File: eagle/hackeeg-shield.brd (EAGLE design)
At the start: 101.6 x 53.3 mm, 144 parts, among them IC1 ADS1299IPAG, IC10 TXB0108PWR, IC11 TXB0108PWR, IC2 TPS72325DBVT, IC3 TPS73225DBVT, IC5 24AA256UID, IC6 TPS60403DBVT, IC7 OPA376DBV, IC8 OPA376DBV, IC9 TXS0102DCUR

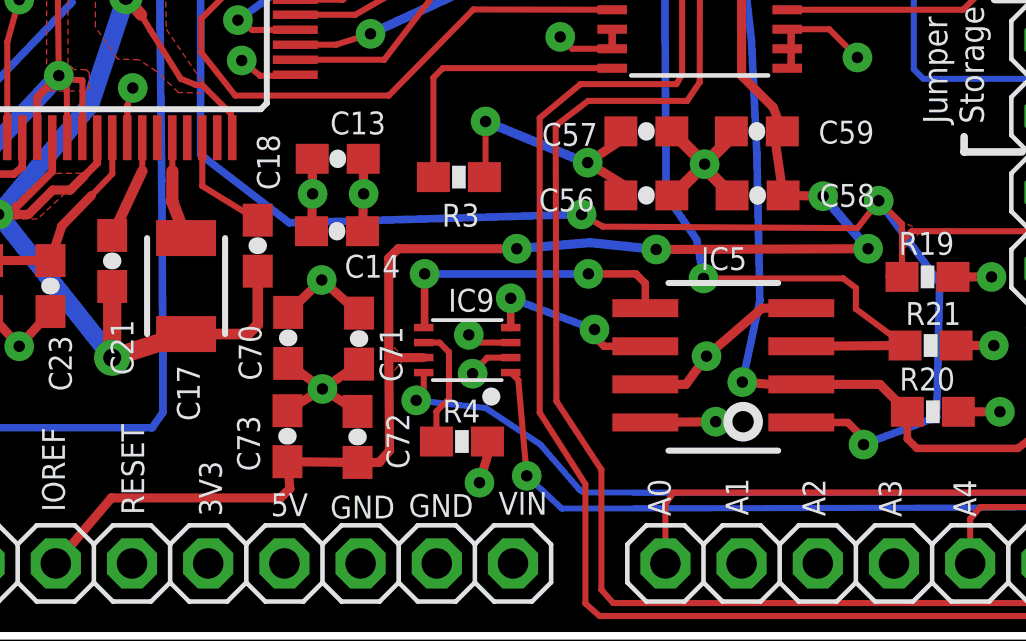
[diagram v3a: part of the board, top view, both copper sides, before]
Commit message: minor via and trace clearance improvements
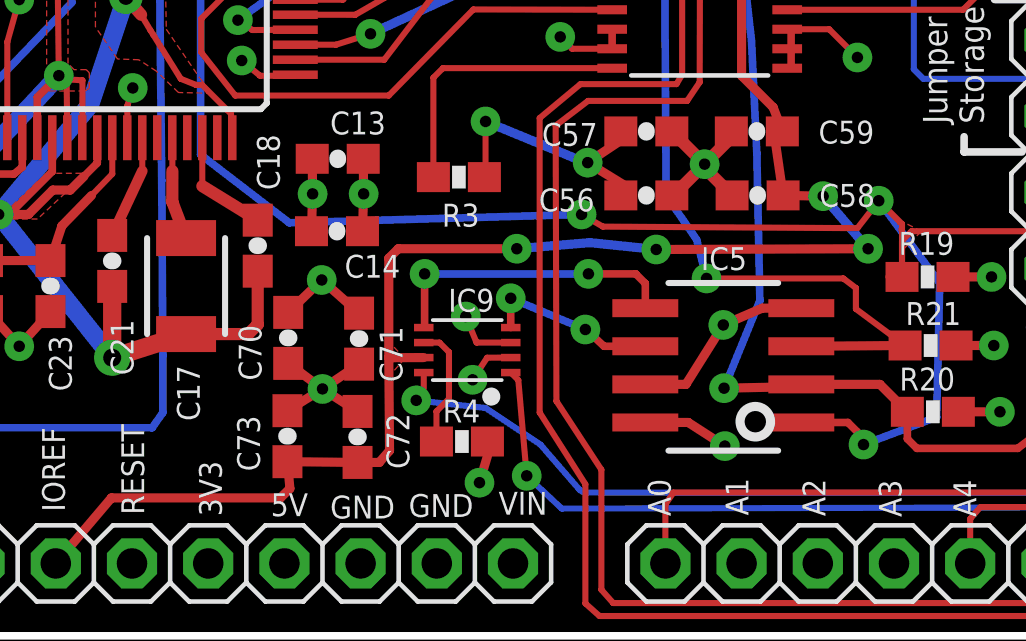
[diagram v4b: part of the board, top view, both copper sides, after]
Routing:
- net DVDD: track 39.8 -> 40.9 mm
- net BOARD_ADDR_1: track 56.2 -> 57.2 mm
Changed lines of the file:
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@@
 <grid distance="4" unitdist="mil" unit="mil" style="lines" multiple="1" display="no" altdistance="0.001" altunitdist="inch" altunit="inch"/>
 <layers>
-<layer number="1" name="Top" color="4" fill="1" visible="no" active="yes"/>
-<layer number="2" name="AGND" color="3" fill="1" visible="no" active="yes"/>
+<layer number="1" name="Top" color="4" fill="1" visible="yes" active="yes"/>
+<layer number="2" name="AGND" color="3" fill="1" visible="yes" active="yes"/>
 <layer number="3" name="Route3" color="4" fill="3" visible="no" active="no"/>
 <layer number="14" name="Route14" color="1" fill="6" visible="no" active="no"/>
-<layer number="15" name="DVDD" color="15" fill="1" visible="no" active="yes"/>
+<layer number="15" name="DVDD" color="15" fill="1" visible="yes" active="yes"/>
 <layer number="16" name="Bottom" color="1" fill="1" visible="yes" active="yes"/>
 <layer number="17" name="Pads" color="2" fill="1" visible="yes" active="yes"/>
@@
 <wire x1="21.1582" y1="44.2722" x2="22.479" y2="44.2722" width="0.254" layer="21"/>
 <wire x1="23.8252" y1="44.2468" x2="25.0444" y2="44.2468" width="0.254" layer="21"/>
-<circle x="53.3908" y="7.2644" radius="0.508" width="0.3048" layer="21"/>
+<circle x="53.7972" y="7.2644" radius="0.508" width="0.3048" layer="21"/>
 </plain>
 <attributes>
@@
 <via x="61.3664" y="33.8582" extent="1-16" drill="0.381"/>
 <wire x1="59.9812" y1="33.0454" x2="61.3664" y2="33.8582" width="0.3556" layer="1"/>
-<wire x1="50.1304" y1="7.239" x2="52.4764" y2="7.2644" width="0.3048" layer="1"/>
-<via x="52.4764" y="7.2644" extent="1-16" drill="0.381"/>
+<wire x1="50.1304" y1="7.239" x2="51.562" y2="7.239" width="0.3048" layer="1"/>
+<wire x1="51.562" y1="7.239" x2="52.7812" y2="6.4516" width="0.3048" layer="1"/>
+<via x="52.7812" y="6.4516" extent="1-16" drill="0.381"/>
 <wire x1="45.646" y1="9.902" x2="44.5048" y2="9.902" width="0.2032" layer="1"/>
-<wire x1="44.5048" y1="9.902" x2="44.2468" y2="10.16" width="0.2032" layer="1"/>
-<via x="44.2468" y="10.16" extent="1-16" drill="0.381"/>
+<wire x1="44.5048" y1="9.902" x2="44.1452" y2="10.7696" width="0.2032" layer="1"/>
+<via x="44.1452" y="10.7696" extent="1-16" drill="0.381"/>
 <wire x1="44.8682" y1="6.604" x2="44.9326" y2="6.3364" width="0.3048" layer="1"/>
 <wire x1="44.9326" y1="6.3364" x2="44.6024" y2="5.2324" width="0.3048" layer="1"/>
@@
 <contactref element="IC1" pad="30"/>
 <wire x1="35.3636" y1="16.7306" x2="35.3636" y2="15.118" width="0.2032" layer="1"/>
-<wire x1="35.3636" y1="15.118" x2="37.211" y2="13.9818" width="0.2032" layer="1"/>
+<wire x1="35.3636" y1="15.118" x2="37.211" y2="13.9818" width="0.4064" layer="1"/>
 </signal>
 <signal name="N$8">
@@
 <wire x1="50.4072" y1="39.116" x2="49.022" y2="39.1414" width="0.4064" layer="1"/>
 <wire x1="45.646" y1="9.402" x2="44.8564" y2="9.398" width="0.2032" layer="1"/>
-<wire x1="44.8564" y1="9.398" x2="44.3738" y2="8.8646" width="0.2032" layer="1"/>
-<via x="44.3738" y="8.8646" extent="1-16" drill="0.381"/>
+<wire x1="44.8564" y1="9.398" x2="44.3738" y2="8.6614" width="0.2032" layer="1"/>
+<via x="44.3738" y="8.6614" extent="1-16" drill="0.381"/>
 <wire x1="38.227" y1="9.2084" x2="39.37" y2="8.3566" width="0.3048" layer="1"/>
 <via x="39.37" y="8.3566" extent="1-16" drill="0.381"/>
@@
 <wire x1="55.3304" y1="11.049" x2="55.372" y2="10.9728" width="0.3048" layer="1"/>
 <wire x1="50.1304" y1="8.509" x2="51.4858" y2="8.509" width="0.3048" layer="1"/>
-<wire x1="51.4858" y1="8.509" x2="52.1716" y2="9.4488" width="0.3048" layer="1"/>
-<via x="52.1716" y="9.4488" extent="1-16" drill="0.381"/>
+<wire x1="51.4858" y1="8.509" x2="52.7304" y2="10.4902" width="0.3048" layer="1"/>
+<via x="52.7304" y="10.4902" extent="1-16" drill="0.381"/>
 <wire x1="55.3304" y1="11.049" x2="54.0258" y2="11.049" width="0.3048" layer="1"/>
-<wire x1="54.0258" y1="11.049" x2="52.1716" y2="9.4488" width="0.3048" layer="1"/>
+<wire x1="54.0258" y1="11.049" x2="52.7304" y2="10.4902" width="0.3048" layer="1"/>
 <wire x1="60.3876" y1="12.0904" x2="61.6712" y2="12.0904" width="0.3048" layer="1"/>
 <via x="61.6712" y="12.0904" extent="1-16" drill="0.381"/>
@@
 <via x="41.3004" y="24.7142" extent="1-16" drill="0.381"/>
 <wire x1="55.3304" y1="8.509" x2="55.2542" y2="8.4328" width="0.3048" layer="1"/>
-<wire x1="55.2542" y1="8.4328" x2="53.3654" y2="8.5852" width="0.3048" layer="1"/>
-<via x="53.3654" y="8.5852" extent="1-16" drill="0.381"/>
-<wire x1="53.3654" y1="8.5852" x2="53.9496" y2="11.303" width="0.254" layer="16"/>
+<wire x1="55.2542" y1="8.4328" x2="52.7558" y2="8.382" width="0.3048" layer="1"/>
+<via x="52.7558" y="8.382" extent="1-16" drill="0.381"/>
+<wire x1="52.7558" y1="8.382" x2="53.9496" y2="11.303" width="0.254" layer="16"/>
 <wire x1="53.9496" y1="11.303" x2="53.848" y2="16.2052" width="0.254" layer="16"/>
 <wire x1="55.3304" y1="8.509" x2="57.951" y2="8.509" width="0.3048" layer="1"/>
@@
 <wire x1="55.3304" y1="9.779" x2="58.7892" y2="9.8044" width="0.3048" layer="1"/>
 <wire x1="50.8254" y1="14.8082" x2="51.8414" y2="13.335" width="0.254" layer="16"/>
-<wire x1="51.8414" y1="13.335" x2="52.07" y2="12.0396" width="0.254" layer="16"/>
-<via x="52.07" y="12.0396" extent="1-16" drill="0.381"/>
-<wire x1="52.07" y1="12.0396" x2="56.7309" y2="12.0396" width="0.2032" layer="1"/>
+<wire x1="51.8414" y1="13.335" x2="52.1716" y2="12.0396" width="0.254" layer="16"/>
+<via x="52.1716" y="12.0396" extent="1-16" drill="0.381"/>
+<wire x1="52.1716" y1="12.0396" x2="56.7309" y2="12.0396" width="0.2032" layer="1"/>
 <wire x1="57.15" y1="11.0236" x2="58.7892" y2="9.8044" width="0.2032" layer="1"/>
 <wire x1="56.7309" y1="12.0396" x2="57.15" y2="11.7221" width="0.2032" layer="1"/>
@@
 <contactref element="IC9" pad="P$4"/>
 <wire x1="50.1304" y1="9.779" x2="48.7553" y2="9.779" width="0.254" layer="1"/>
-<wire x1="48.7553" y1="9.779" x2="48.4378" y2="10.0965" width="0.254" layer="1"/>
-<wire x1="48.4378" y1="10.0965" x2="48.4378" y2="10.3378" width="0.254" layer="1"/>
-<via x="48.4378" y="10.3378" extent="1-16" drill="0.381"/>
-<wire x1="48.4378" y1="10.3378" x2="45.6438" y2="11.3792" width="0.254" layer="16"/>
+<wire x1="48.7553" y1="9.779" x2="48.4124" y2="10.0965" width="0.254" layer="1"/>
+<wire x1="48.4124" y1="10.0965" x2="48.133" y2="10.3378" width="0.254" layer="1"/>
+<via x="48.133" y="10.3378" extent="1-16" drill="0.381"/>
+<wire x1="48.133" y1="10.3378" x2="45.6438" y2="11.3792" width="0.254" layer="16"/>
 <via x="45.6438" y="11.3792" extent="1-16" drill="0.381"/>
 <wire x1="45.6438" y1="11.3792" x2="45.646" y2="10.402" width="0.254" layer="1"/>
@@
 <contactref element="C20" pad="2"/>
 <contactref element="C21" pad="2"/>
-<wire x1="37.211" y1="12.2818" x2="37.211" y2="10.5031" width="0.3556" layer="1"/>
-<wire x1="37.211" y1="10.5031" x2="36.8935" y2="10.1856" width="0.3556" layer="1"/>
-<wire x1="36.8935" y1="10.1856" x2="34.8234" y2="10.1856" width="0.3556" layer="1"/>
+<wire x1="37.211" y1="12.2818" x2="37.211" y2="10.5031" width="0.4064" layer="1"/>
+<wire x1="37.211" y1="10.5031" x2="36.8935" y2="10.1856" width="0.4064" layer="1"/>
+<wire x1="36.8935" y1="10.1856" x2="34.8234" y2="10.1856" width="0.4064" layer="1"/>
 <wire x1="29.5656" y1="14.1732" x2="28.9306" y2="14.1732" width="0.3048" layer="1"/>
 <wire x1="26.5294" y1="14.1732" x2="26.5294" y2="11.7602" width="0.4064" layer="1"/>

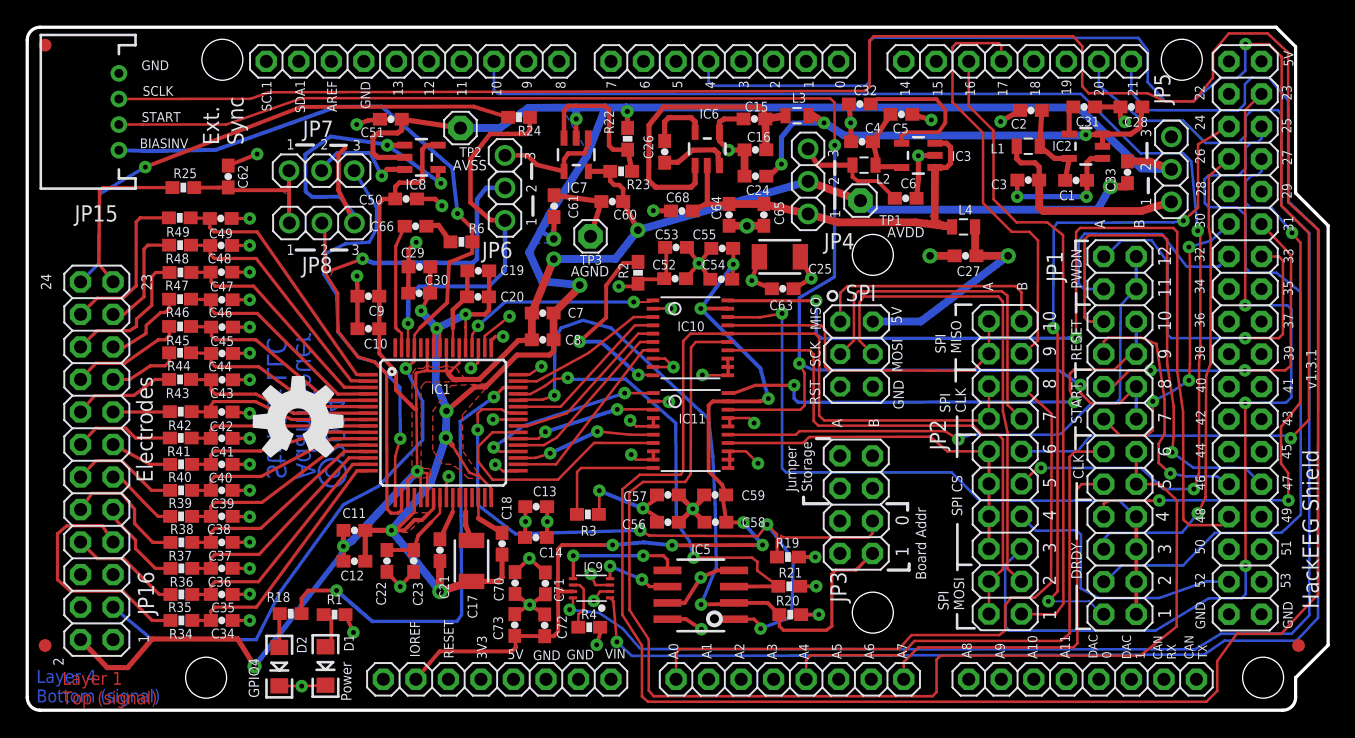
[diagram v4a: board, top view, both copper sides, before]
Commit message: added AVSS polygon to bottom layer to join disconnected AVSS segments; widened a lot of AVDD and AVSS traces
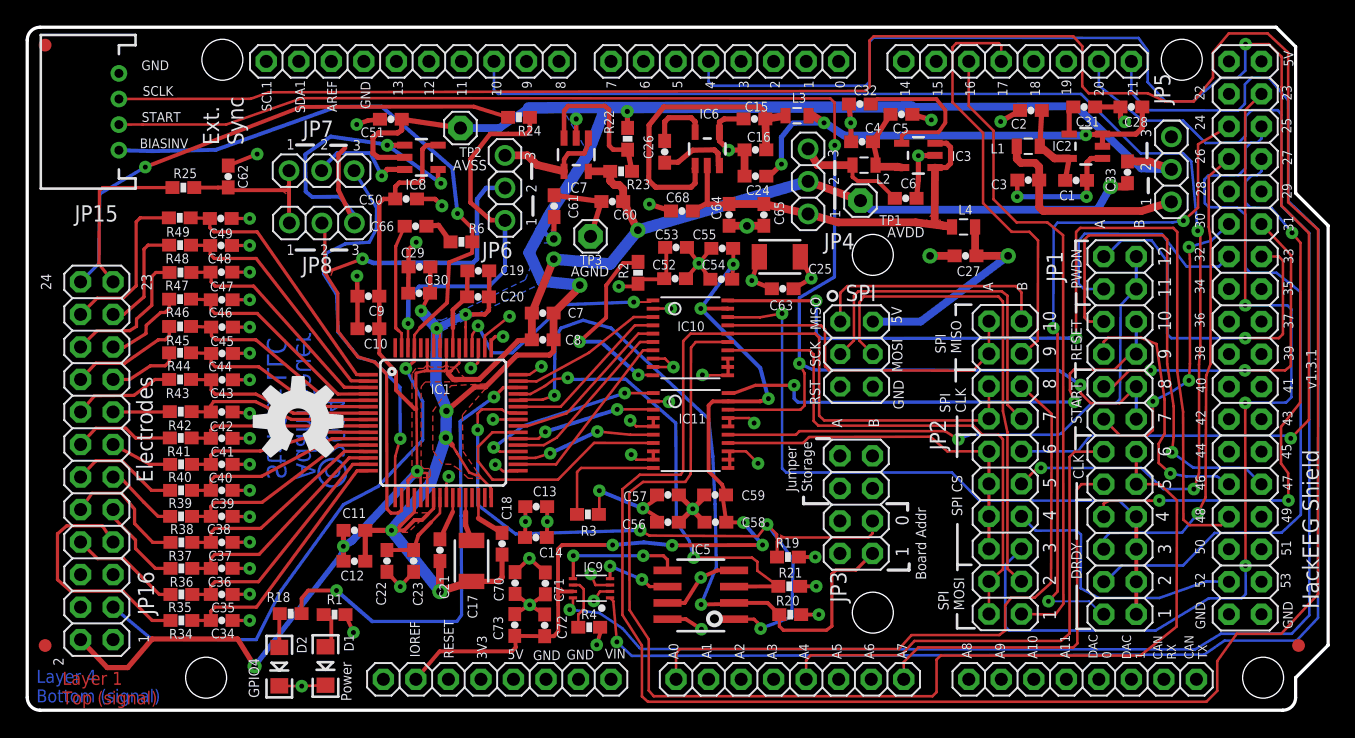
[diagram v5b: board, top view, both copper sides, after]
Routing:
- net CLKSEL: track 16.3 -> 18.3 mm
